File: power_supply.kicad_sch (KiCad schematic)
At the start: 50 parts, among them Q1 AO4407A, Q2 SI4178DY-T1-GE3, Q3 AO4407A, U1 BQ7791500PWR, U2 LTC4007

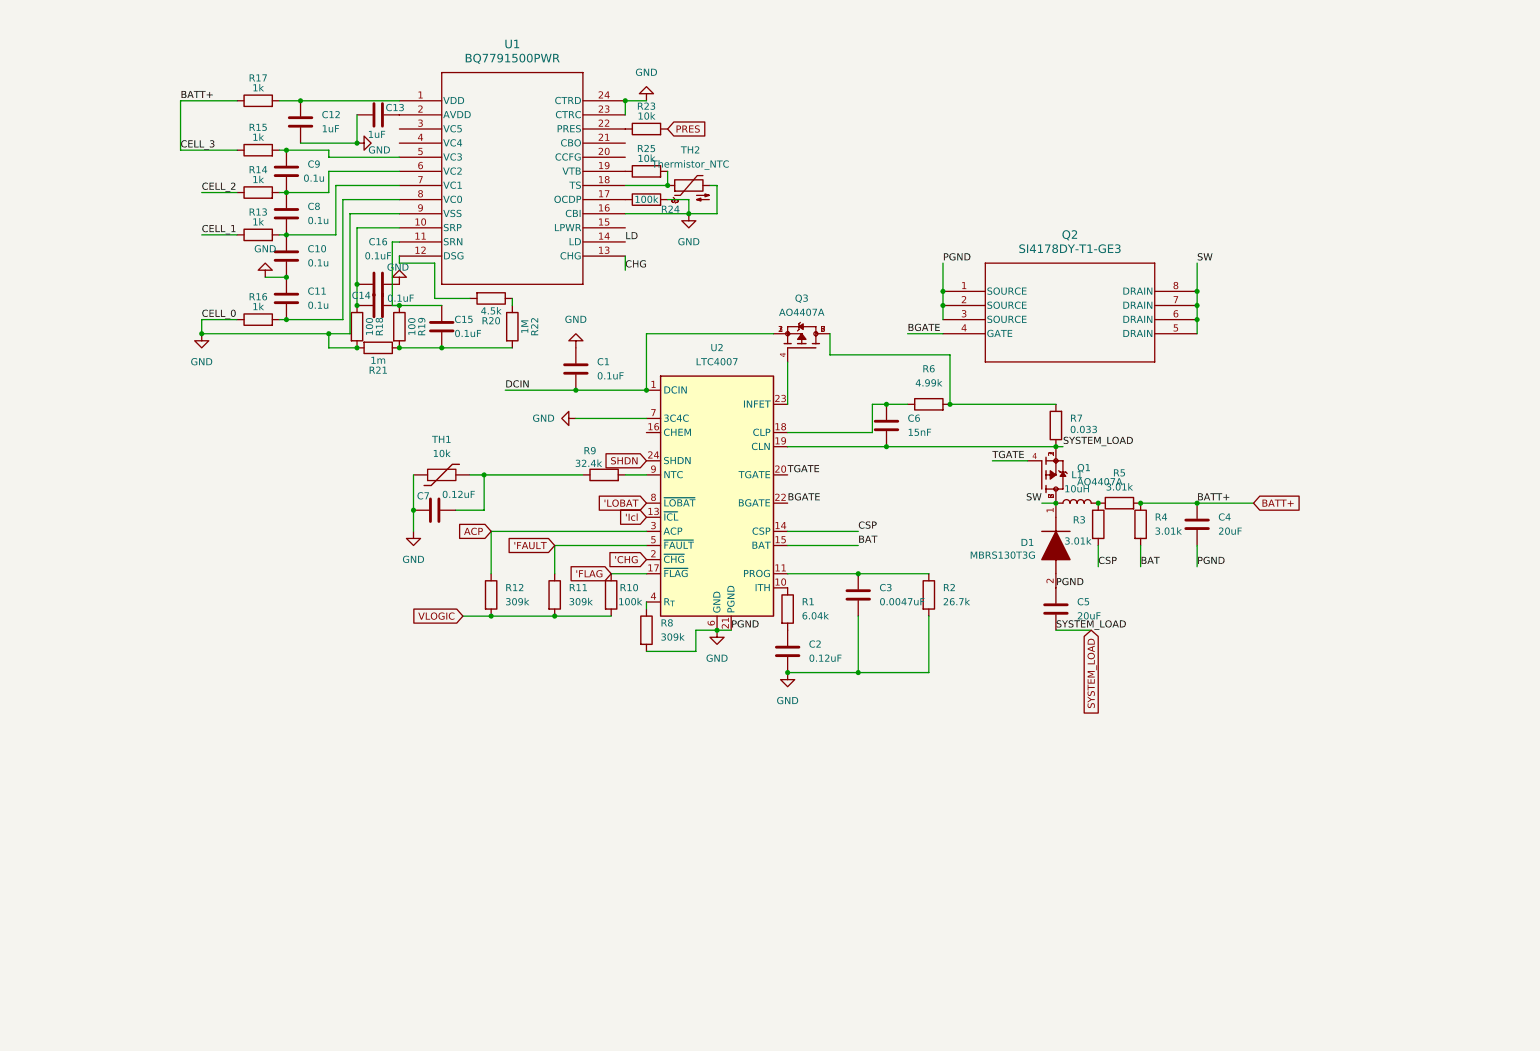
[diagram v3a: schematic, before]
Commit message: power supply schematic done
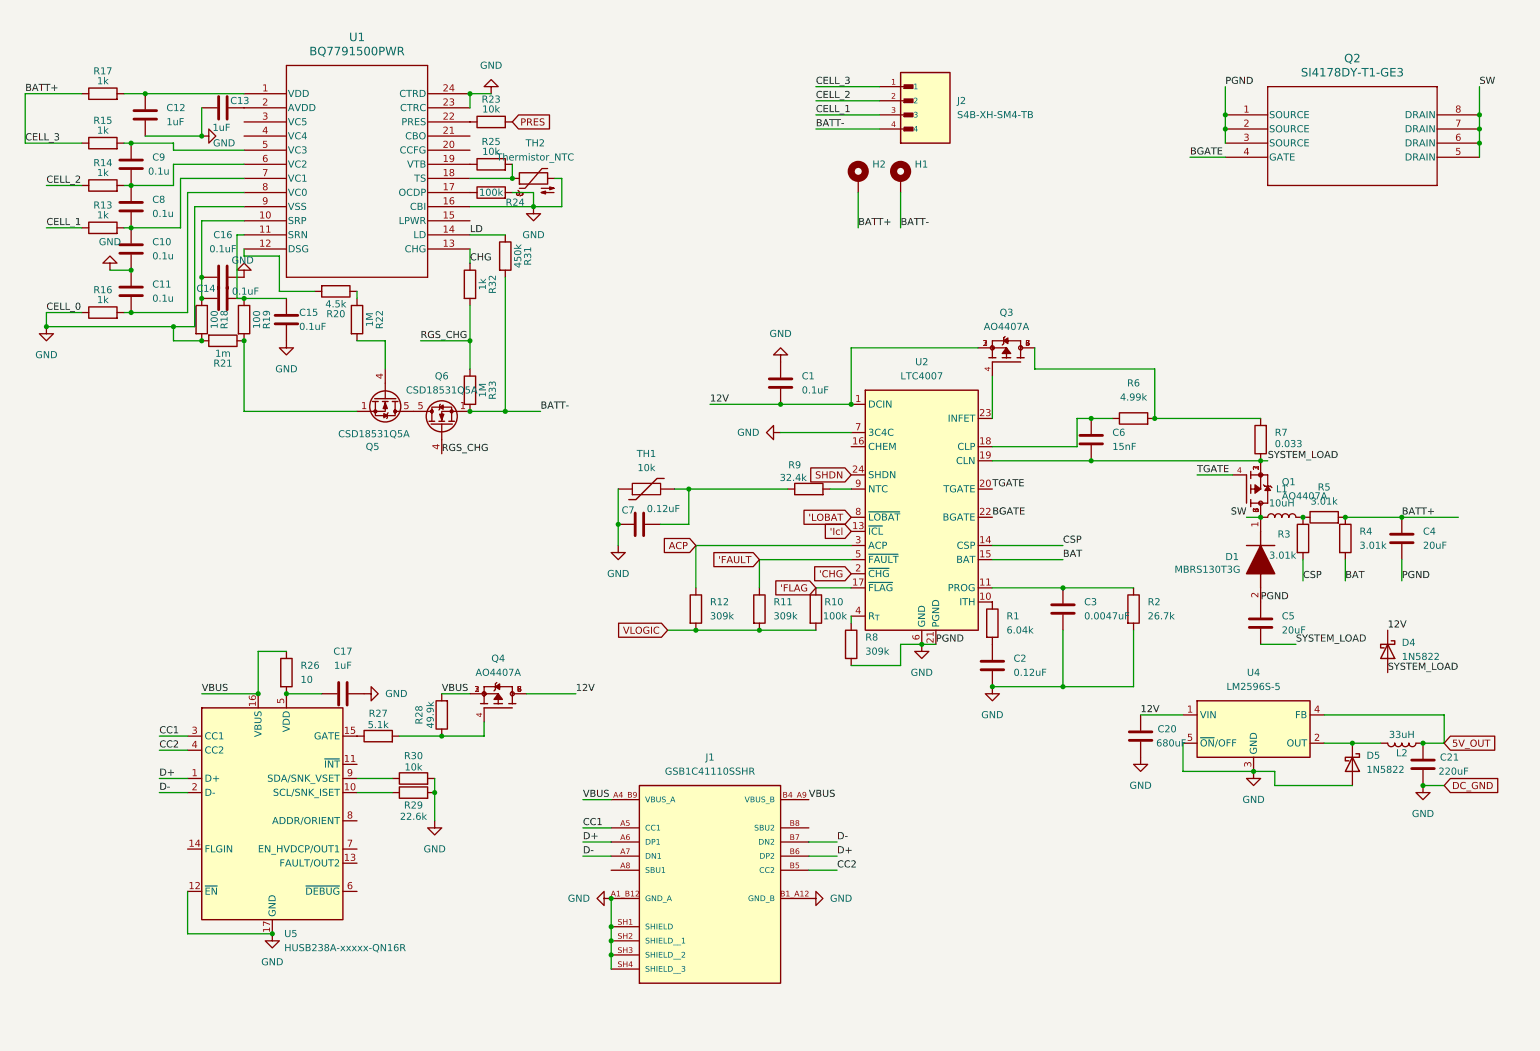
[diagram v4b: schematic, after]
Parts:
- added C17: 1uF, Capacitor_SMD:C_0805_2012Metric_Pad1.18x1.45mm_HandSolder, symbol Device:C
- added C20: 680uF, Capacitor_SMD:C_0805_2012Metric_Pad1.18x1.45mm_HandSolder, symbol Device:C
- added C21: 220uF, Capacitor_SMD:C_0805_2012Metric_Pad1.18x1.45mm_HandSolder, symbol Device:C
- added D4, D5: 1N5822, Diode_THT:D_DO-201AD_P15.24mm_Horizontal, symbol Diode:1N5822
- added H1, H2: MountingHole_Pad_MP, symbol Mechanical:MountingHole_Pad_MP
- added J1: GSB1C41110SSHR, GSB1C41110SSHR:AMPHENOL_GSB1C41110SSHR, symbol GSB1C41110SSHR:GSB1C41110SSHR
- added J2: S4B-XH-SM4-TB, S4B-XH-SM4-TB:JST_S4B-XH-SM4-TB, symbol S4B-XH-SM4-TB:S4B-XH-SM4-TB
- added L2: 33uH, Inductor_SMD:L_0805_2012Metric_Pad1.15x1.40mm_HandSolder, symbol Device:L
- added Q4: AO4407A, AO4407A:SOIC127P600X175-8N, symbol AO4407A:AO4407A
- added Q5, Q6: CSD18531Q5A, Package_TO_SOT_SMD:TDSON-8-1, symbol Transistor_FET:CSD18531Q5A
- added R26: 10, Resistor_SMD:R_0805_2012Metric_Pad1.20x1.40mm_HandSolder, symbol Device:R
- added R27: 5.1k, Resistor_SMD:R_0805_2012Metric_Pad1.20x1.40mm_HandSolder, symbol Device:R
- added R28: 49.9k, Resistor_SMD:R_0805_2012Metric_Pad1.20x1.40mm_HandSolder, symbol Device:R
- added R29: 22.6k, Resistor_SMD:R_0805_2012Metric_Pad1.20x1.40mm_HandSolder, symbol Device:R
- added R30: 10k, Resistor_SMD:R_0805_2012Metric_Pad1.20x1.40mm_HandSolder, symbol Device:R
- added R31: 450k, Resistor_SMD:R_0805_2012Metric_Pad1.20x1.40mm_HandSolder, symbol Device:R
- added R32: 1k, Resistor_SMD:R_0805_2012Metric_Pad1.20x1.40mm_HandSolder, symbol Device:R
- added R33: 1M, Resistor_SMD:R_0805_2012Metric_Pad1.20x1.40mm_HandSolder, symbol Device:R
- added U4: LM2596S-5, Package_TO_SOT_SMD:TO-263-5_TabPin3, symbol Regulator_Switching:LM2596S-5
- added U5: HUSB238A-xxxxx-QN16R, Package_DFN_QFN:WQFN-16-1EP_3x3mm_P0.5mm_EP1.75x1.75mm, symbol Interface_USB:HUSB238A-xxxxx-QN16R
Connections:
- net BATT+: now also H2.MP, J2.1
- net CELL_1: now also J2.3
- net CELL_2: now also J2.2
- net CHG: now also R32.1
- net GND: now also C15.2, C17.2, C20.2, C21.2, D5.2 (A), J1.A1_B12 (GND_A), J1.B1_A12 (GND_B), J1.SH1 (SHIELD), J1.SH2 (SHIELD__1), J1.SH3 (SHIELD__2), J1.SH4 (SHIELD__3), R29.2, R30.2, U4.3 (GND), U4.5 (~{ON}/OFF), U5.12 (~{EN}), U5.17 (GND)
- net LD: now also R31.1
- net SYSTEM_LOAD: now also D4.2 (A)
- net at R19.2, R21.1: now also Q5.1 (S), Q5.2 (S), Q5.3 (S); no longer C15.2, R22.2
- net DCIN renamed 12V
- net 12V: now also C20.1, D4.1 (K), Q4.5, Q4.6, Q4.7, Q4.8, U4.1 (VIN)
- new net: Q4.4, R27.2, R28.1
- new net: Q5.4 (G), R22.2
- new net: Q5.5 (D), Q6.5 (D)
- new net: R29.1, U5.10 (SCL/SNK_ISET)
- new net: R27.1, U5.15 (GATE)
- new net: C17.1, R26.2, U5.5 (VDD)
- new net: R30.1, U5.9 (SDA/SNK_VSET)
- new net: D5.1 (K), L2.2, U4.2 (OUT)
- new net 5V_OUT: C21.1, L2.1, U4.4 (FB)
- new net BATT-: H1.MP, J2.4, Q6.1 (S), Q6.2 (S), Q6.3 (S), R31.2, R33.2
- new net CC1: J1.A5 (CC1), U5.3 (CC1)
- new net CC2: J1.B5 (CC2), U5.4 (CC2)
- new net D+: J1.A6 (DP1), J1.B6 (DP2), U5.1 (D+)
- new net D-: J1.A7 (DN1), J1.B7 (DN2), U5.2 (D-)
- new net RGS_CHG: Q6.4 (G), R32.2, R33.1
- new net VBUS: J1.A4_B9 (VBUS_A), J1.B4_A9 (VBUS_B), Q4.1, Q4.2, Q4.3, R26.1, R28.2, U5.16 (VBUS)
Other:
- moved on the sheet: C1, C10, C11, C12, C13, C14, C15, C16, C2, C3, C4, C5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

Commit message: add shcematic labels
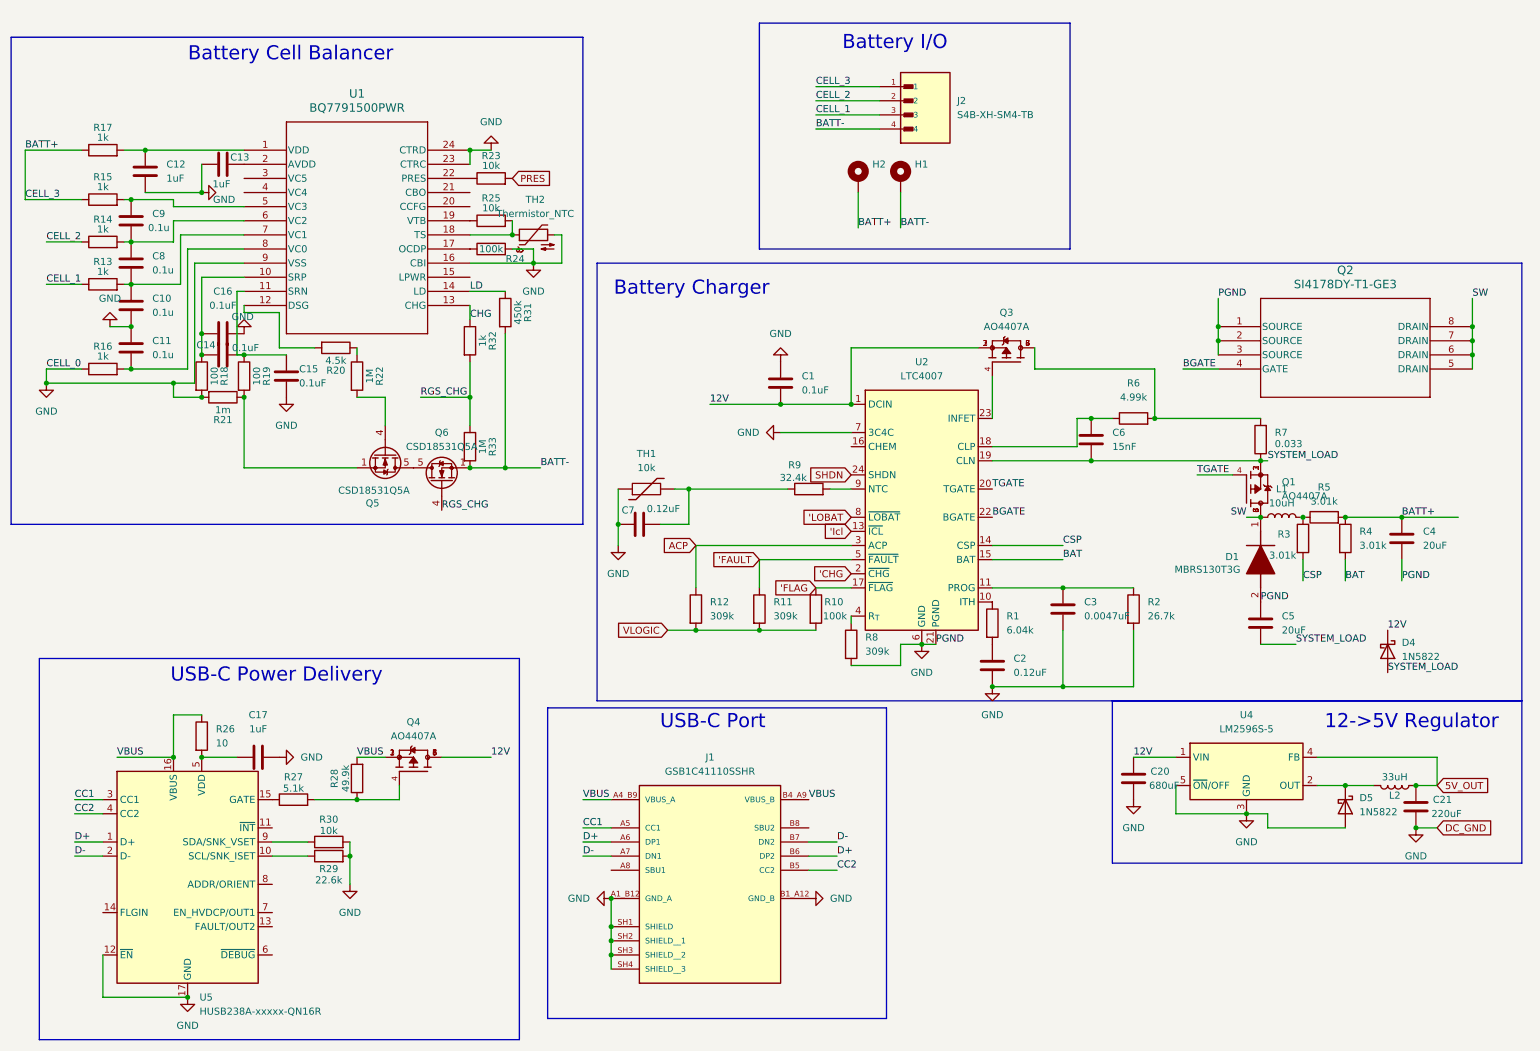
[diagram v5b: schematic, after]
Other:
- note added: "12->5V Regulator"
- note added: "Battery Cell Balancer"
- note added: "Battery Charger"
- note added: "Battery I/O"
- note added: "USB-C Port"
- note added: "USB-C Power Delivery"
- moved on the sheet: C10, C11, C12, C13, C14, C15, C16, C17, C20, C21, C8, C9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

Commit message: footprint issues solved
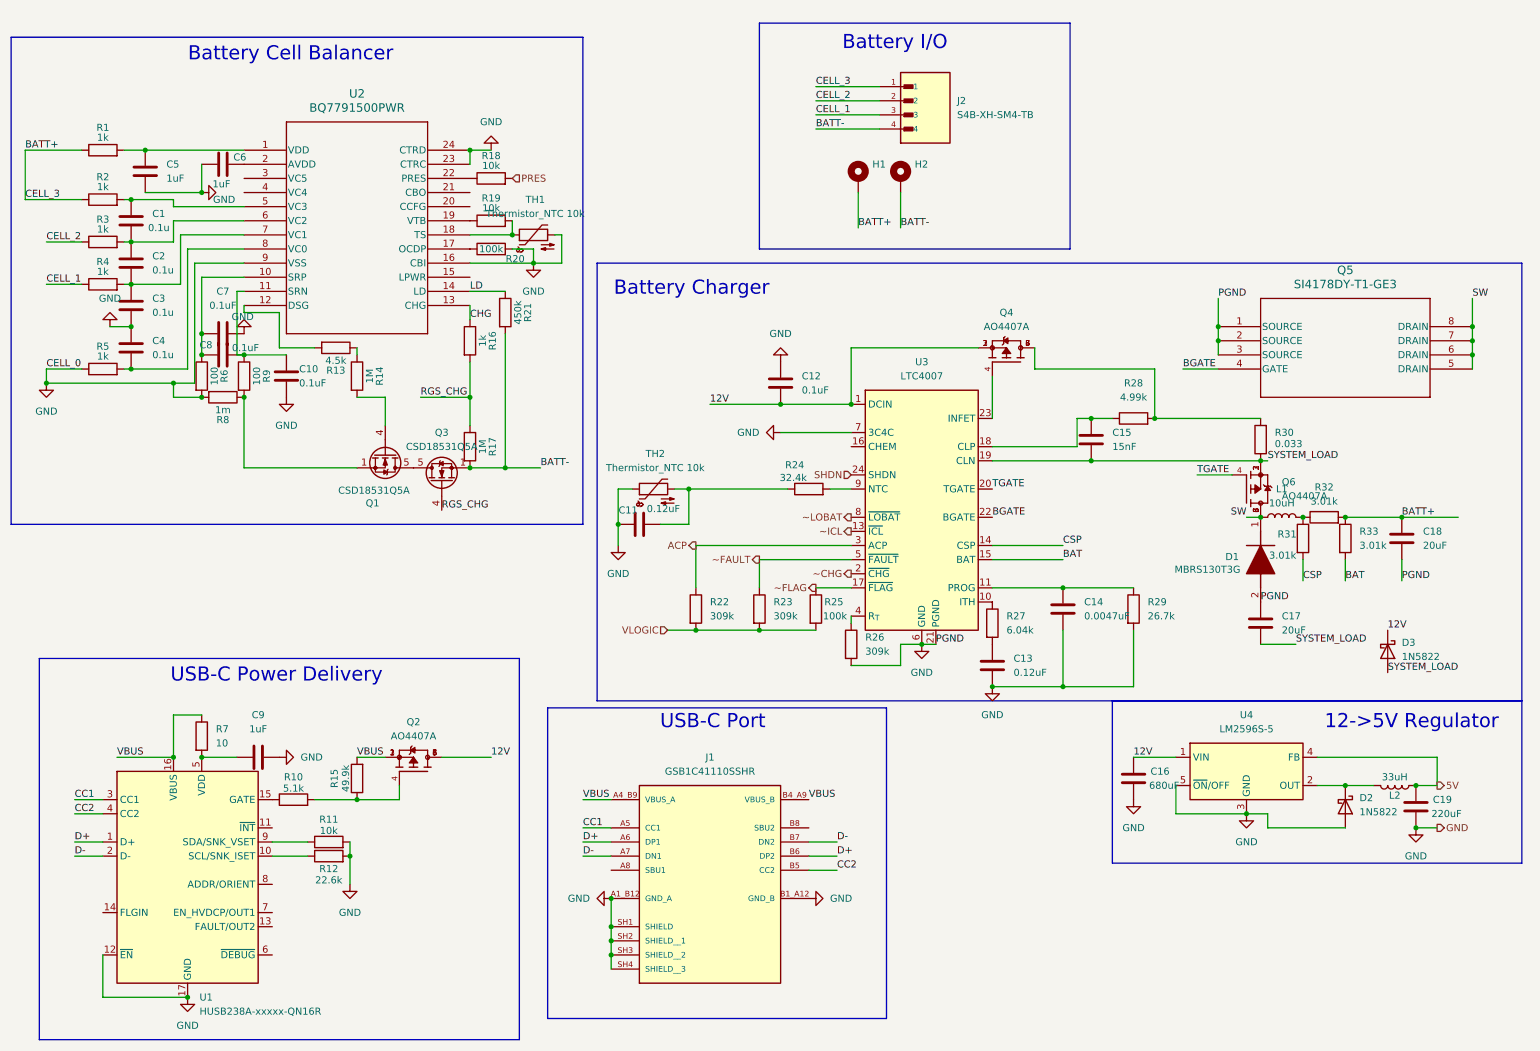
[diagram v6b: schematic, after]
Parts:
- removed TH1: 10k, Resistor_SMD:R_0805_2012Metric_Pad1.20x1.40mm_HandSolder, symbol Device:Thermistor
- added TH2: Thermistor_NTC 10k, Resistor_SMD:R_0402_1005Metric_Pad0.72x0.64mm_HandSolder, symbol Device:Thermistor_NTC
- J2: footprint S4B-XH-SM4-TB:JST_S4B-XH-SM4-TB -> S4B_XH_SM4_TB:JST_S4B-XH-SM4-TB
- TH1: renamed from TH2; value Thermistor_NTC -> Thermistor_NTC 10k; footprint (none) -> Resistor_SMD:R_0402_1005Metric_Pad0.72x0.64mm_HandSolder
- renumbered C9 to C1, C15 to C10, C7 to C11, C1 to C12, C2 to C13, C3 to C14, C6 to C15, C20 to C16, C5 to C17, C4 to C18, C21 to C19, C8 to C2, C10 to C3, C11 to C4, C12 to C5, C13 to C6, C16 to C7, C14 to C8, C17 to C9, D5 to D2, D4 to D3, H2 to H1, H1 to H2, Q5 to Q1, Q4 to Q2, Q6 to Q3, Q3 to Q4, Q2 to Q5, Q1 to Q6, R17 to R1, R27 to R10, R30 to R11, R29 to R12, R20 to R13, R22 to R14, R28 to R15, R32 to R16, R33 to R17, R23 to R18, R25 to R19, R15 to R2, R24 to R20, R31 to R21, R12 to R22, R11 to R23, R9 to R24, R10 to R25, R8 to R26, R1 to R27, R6 to R28, R2 to R29, R14 to R3, R7 to R30, R3 to R31, R5 to R32, R4 to R33, R13 to R4, R16 to R5, R18 to R6, R26 to R7, R21 to R8, R19 to R9, U5 to U1, U1 to U2, U2 to U3
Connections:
- net GND: now also TH2.1
- net at C11.2, R24.1: now also TH2.2
- net 'CHG renamed ~CHG
- net 'FAULT renamed ~FAULT
- net 'FLAG renamed ~FLAG
- net 'Icl renamed ~ICL
- net 'LOBAT renamed ~LOBAT
- net 5V_OUT renamed 5V

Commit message: started layout
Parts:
- removed D2, D3: 1N5822, Diode_THT:D_DO-201AD_P15.24mm_Horizontal, symbol Diode:1N5822
- removed H1, H2: MountingHole_Pad_MP, symbol Mechanical:MountingHole_Pad_MP
- added D2, D3: MBRS130T3G, DIOM5436X247N, symbol MBRS130T3G:MBRS130T3G
- added D4: 1655, 1655:LED_1655, symbol 1655:1655
- added J4: ~, Battery_Connector:LiPo Wire Pads, symbol SWM Components:Battery_Connectors
- added S1, S3: 100SP1T1B4M2QE, Switches:SW_100SP1T1B4M2QE, symbol Switch_SWM:100SP1T1B4M2QE
- added U6: SN74LVC1T45DCK, Package_TO_SOT_SMD:SOT-363_SC-70-6, symbol Logic_LevelTranslator:SN74LVC1T45DCK
- J2: footprint S4B_XH_SM4_TB:JST_S4B-XH-SM4-TB -> S4B-XH-SM4-TB:JST_S4B-XH-SM4-TB
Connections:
- net 12V: now also D3.1 (K)
- net 5V: now also D4.3 (VDD), U6.5 (DIR), U6.6 (VCCB)
- net GND: now also J2.4, U2.20 (CCFG), D2.2 (A), D4.1 (VSS), U6.2 (GND); no longer U2.16 (CBI)
- net PRES: now also C5.1, R1.2, U2.1 (VDD)
- net SYSTEM_LOAD: now also D3.2 (A)
- net VBUS: now also S1.1; no longer J1.A4_B9 (VBUS_A), J1.B4_A9 (VBUS_B)
- net VLOGIC: now also U6.1 (VCCA)
- net at C1.1, R2.2, U2.5 (VC3): now also U2.3 (VC5), U2.4 (VC4)
- net at L2.2, U4.2 (OUT): now also D2.1 (K)
- net BATT+ renamed CELL_3
- net CELL_3: now also S3.1
- net BATT- renamed PACK-
- net PACK-: now also J4.2 (PACK-); no longer J2.4
- new net: D4.2 (DIN), U6.4 (B)
- new net NEOPIXEL: U6.3 (A)
- new net PACK+: J4.1 (PACK+), S3.2
- new net USB_VBUS: J1.A4_B9 (VBUS_A), J1.B4_A9 (VBUS_B), S1.2
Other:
- moved on the sheet: J2

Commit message: done
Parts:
- removed C16: 680uF, Capacitor_SMD:C_0805_2012Metric_Pad1.18x1.45mm_HandSolder, symbol Device:C
- removed L1: 10uH, Inductor_SMD:L_0805_2012Metric_Pad1.05x1.20mm_HandSolder, symbol Device:L
- removed L2: 33uH, Inductor_SMD:L_0805_2012Metric_Pad1.15x1.40mm_HandSolder, symbol Device:L
- added C16: UCL1E681MNL1GS, 680:CAPAE1030X1350N, symbol 680:UCL1E681MNL1GS
- added L3: NR6045T100M, NR6045T100M:IND_NR6045T100M, symbol NR6045T100M:NR6045T100M
- added L4: SRN8040-330M, SRN8040:IND_BOURNS_SRN8040, symbol SRN8040-330M:SRN8040-330M
- C1, C10, C11, C12, C13, C2, C3, C4, C7, C8: footprint Capacitor_SMD:C_0805_2012Metric_Pad1.18x1.45mm_HandSolder -> LED_SMD:LED_0805_2012Metric_Pad1.15x1.40mm_HandSolder
- C14, C15, C5, C6, C9: footprint Capacitor_SMD:C_0805_2012Metric_Pad1.18x1.45mm_HandSolder -> Capacitor_SMD:C_0603_1608Metric_Pad1.08x0.95mm_HandSolder
- C19: footprint Capacitor_SMD:C_0805_2012Metric_Pad1.18x1.45mm_HandSolder -> Capacitor_SMD:C_1206_3216Metric_Pad1.33x1.80mm_HandSolder
- R13: value 4.5k -> 4k
- R30: value 0.033 -> 0.025
- R32: value 3.01k -> 0.025
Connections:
- net 12V: now also C16.A
- net 5V: now also L4.1
- net GND: now also C16.C
- net SW: now also L3.1
- net at R31.1, R32.1: now also L3.2
- net at Q1.1 (S), Q1.2 (S), Q1.3 (S)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: now also R14.2
- net at Q1.4 (G): now also R13.1, R14.1; no longer R14.2
- net at D2.1 (K), U4.2 (OUT): now also L4.2
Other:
- moved on the sheet: C18, C19, R31, R32, R33
